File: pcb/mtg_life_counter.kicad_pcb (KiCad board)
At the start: 2 copper layers, 167.6 x 101.6 mm, 121 parts, among them J1 USB C 4907, J2 ICSP, J3 TP_UART, Q1 DMG2301L, Q10 DMG2301L, Q11 DMG2301L, Q12 DMG2301L, Q13 DMG2301L, Q14 DMG2301L, Q15 DMG2301L, Q16 DMG2301L, Q2 DMG2301L, Q3 DMG2301L, Q4 DMG2301L, Q5 DMG2301L, Q6 DMG2301L, Q7 DMG2301L, Q8 DMG2301L, Q9 DMG2301L, SW1 SW_SPST, SW2 SW_SPST, U1 ATmega328P-AU, U2 TPIC6C596, U3 TPIC6C596, U4 TPIC6C596, U5 TPIC6C596, Y1 16MHz

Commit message: start to route display traces
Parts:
- removed the R20 at (110.2, 36.0)
- removed the R33 at (174.9, 35.6)
- removed the R46 at (167.3, 167.2)
- removed R59: 10k, Resistor_SMD:R_0805_2012Metric_Pad1.20x1.40mm_HandSolder
- H1, H2, H3, H4: footprint MountingHole:MountingHole_3.2mm_M3_Pad_Via -> MountingHole:MountingHole_3.2mm_M3
- moved C7 116.2 mm to (189.2, 81.0), turned to -90 degrees
- moved H4 107.1 mm to (55.9, 147.3)
- moved C6 78.7 mm to (125.7, 81.0), turned to -90 degrees
- moved R47 65.8 mm to (139.1, 120.4), turned to -90 degrees
- moved R8 61.0 mm to (131.4, 82.8), turned to 90 degrees
- moved R9 59.9 mm to (134.0, 82.8), turned to 90 degrees
- moved C9 59.3 mm to (125.7, 119.1), turned to -90 degrees
- moved Q15 59.1 mm to (130.5, 127.3), turned to -90 degrees
- moved C8 59.1 mm to (189.2, 119.1), turned to -90 degrees
- moved R10 59.0 mm to (136.5, 82.8), turned to 90 degrees
- moved R46 58.7 mm to (131.4, 120.4), turned to -90 degrees
- moved R11 58.3 mm to (139.1, 82.8), turned to 90 degrees
- moved R45 58.0 mm to (134.0, 120.4), turned to -90 degrees
- moved R44 57.5 mm to (136.5, 120.4), turned to -90 degrees
- moved Q1 56.7 mm to (130.5, 75.9), turned to -90 degrees
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- renumbered C7 to C6, C6 to C7, D2 to D1, D3 to D2, D4 to D3, D5 to D4, D1 to D5, R21 to R20, R22 to R21, R23 to R22, R24 to R23, R25 to R24, R26 to R25, R27 to R26, R28 to R27, R29 to R28, R30 to R29, R31 to R30, R32 to R31, R34 to R32, R35 to R33, R36 to R34, R37 to R35, R38 to R36, R39 to R37, R40 to R38, R41 to R39, R42 to R40, R43 to R41, R44 to R42, R45 to R43, R47 to R44, R48 to R45, R49 to R46, R50 to R47, R51 to R48, R52 to R49, R53 to R50, R54 to R51, R55 to R52, R56 to R53, R57 to R54, R58 to R55
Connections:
- net /D1(TX) renamed /TX
- J3 pad 1: /D0(RX) -> unconnected-(J3-Pin_1-Pad1)
- U2 pad 7: Net-(U2-~{SRCLR}) -> +5V
- U3 pad 7: Net-(U3-~{SRCLR}) -> +5V
- U4 pad 7: Net-(U4-~{SRCLR}) -> +5V
- U5 pad 7: Net-(U5-~{SRCLR}) -> +5V
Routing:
- net +5V: track 0.00 -> 90.7 mm, vias 0 -> 2
- net /P2/CA1: track 0.00 -> 39.4 mm, vias 0 -> 2
- net /P4/CA1: track 0.00 -> 38.6 mm, vias 0 -> 2
- net /P1/CA3: track 0.00 -> 37.2 mm, vias 0 -> 2
- net /P3/CA3: track 0.00 -> 36.9 mm, vias 0 -> 2
- net /P3/CA4: track 0.00 -> 35.5 mm, vias 0 -> 2
- net /P1/CA4: track 0.00 -> 35.5 mm, vias 0 -> 2
- net Net-(Q12-G): track 0.00 -> 34.2 mm, vias 0 -> 2
- net /P1/CA2: track 0.00 -> 32.8 mm, vias 0 -> 2
- net /P2/SB: track 0.00 -> 32.8 mm, vias 0 -> 2
- net /P1/SB: track 0.00 -> 32.8 mm, vias 0 -> 2
- net /P3/CA2: track 0.00 -> 32.5 mm, vias 0 -> 2
- net /P2/CA2: track 0.00 -> 29.9 mm, vias 0 -> 2
- net /P2/SG: track 0.00 -> 29.8 mm, vias 0 -> 2
- net /P1/SG: track 0.00 -> 29.7 mm, vias 0 -> 2
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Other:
- board text added: "Max Proskauer v3.0 Jan 2026 github.com/mprosk/mtg_life_counter"
- board text added: "Version 3.0"
- board text removed: "Max Proskauer v2.0 Dec 2021 github.com/mprosk/mtg_life_counter"
- board text removed: "Version 2.0"

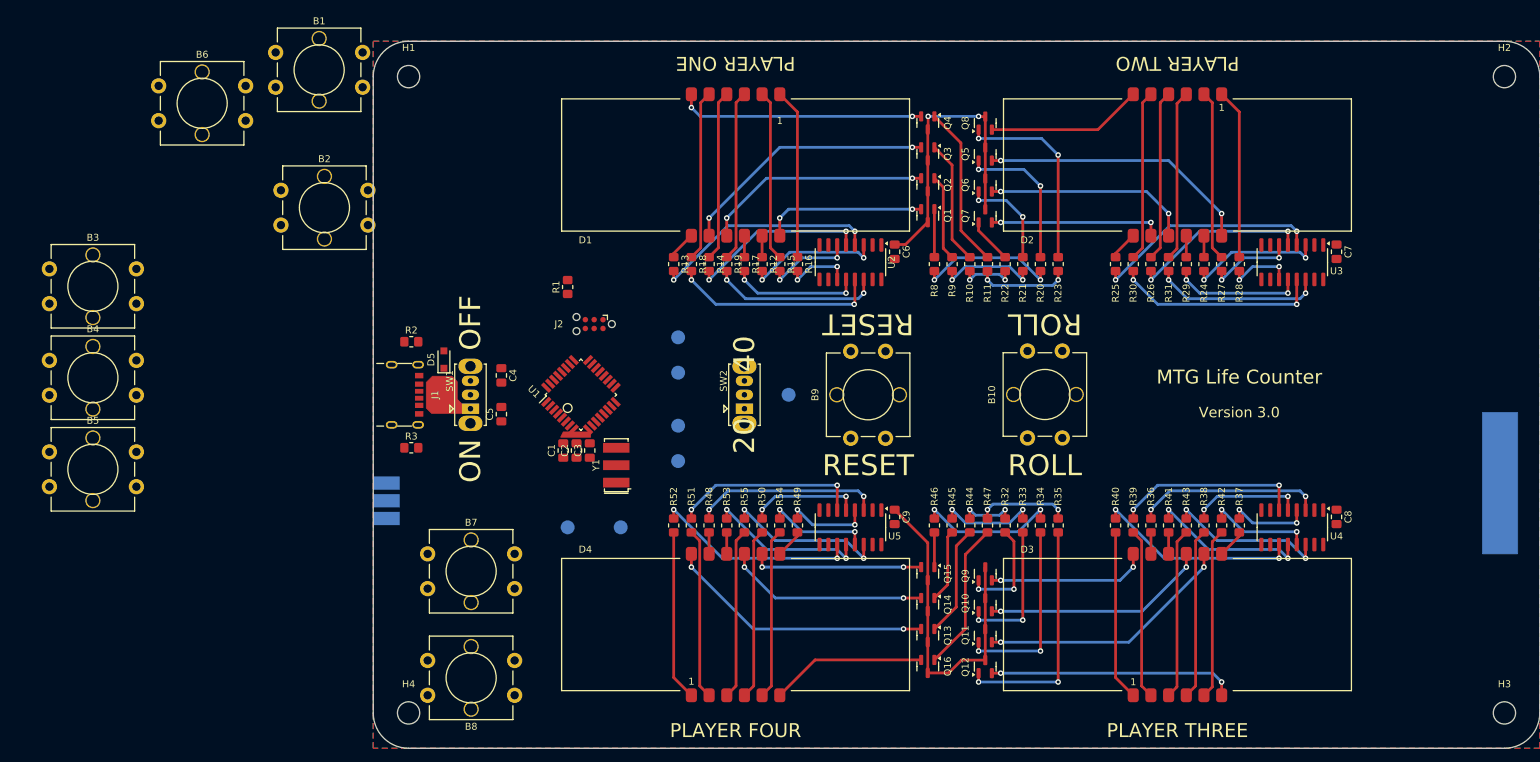
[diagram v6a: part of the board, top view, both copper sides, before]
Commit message: switch to all smd components
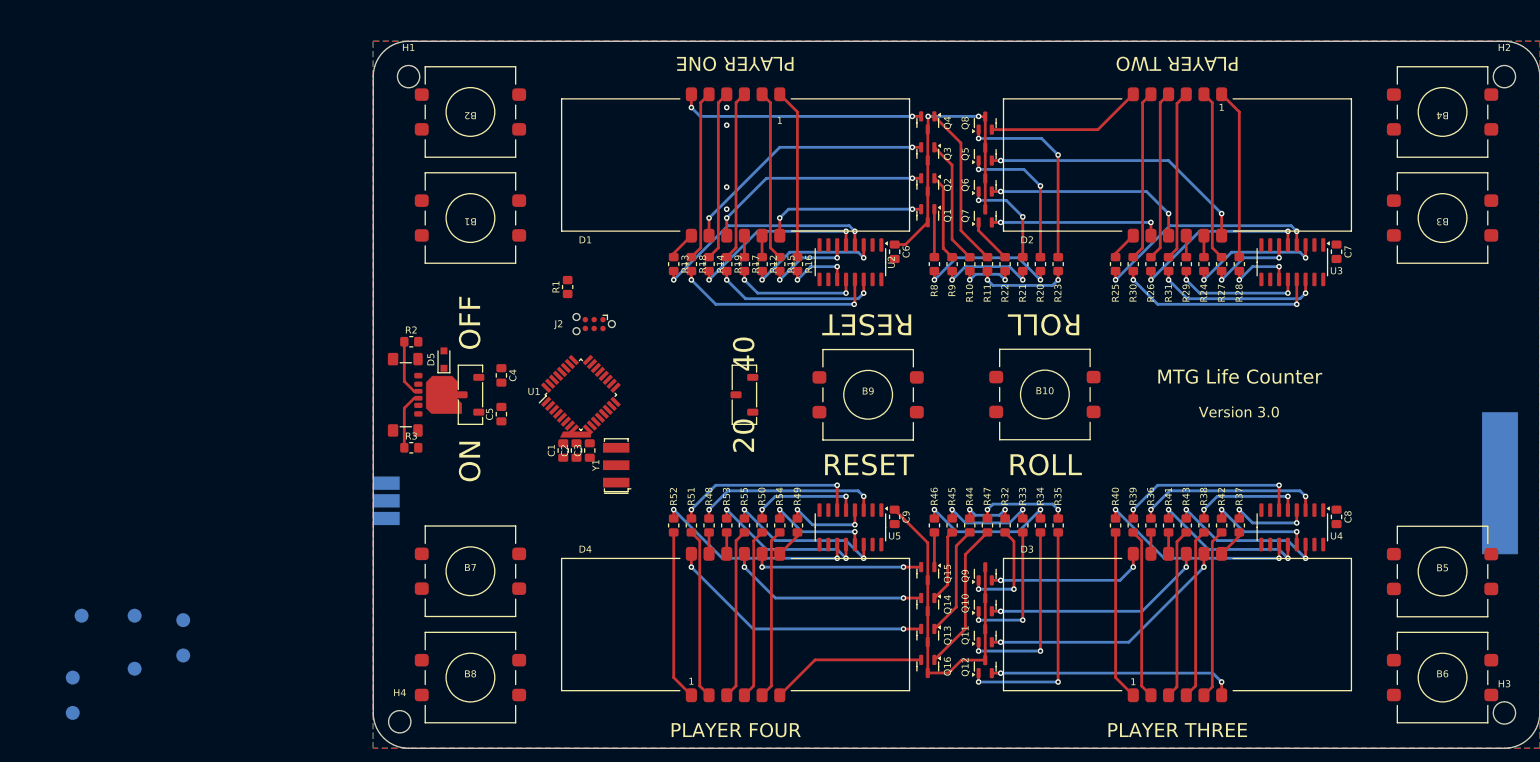
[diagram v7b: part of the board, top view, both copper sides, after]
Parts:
- B1, B10, B2, B3, B4, B5, B6, B7, B8, B9: footprint mtg_life_counter:B3F_12mm -> mtg_life_counter:SW_SPST_WE_WS-TASV_12mm_Tac
- J1: value USB C 4907 -> GCT USB-4135-GF-A; footprint mtg_life_counter:4907_USB_C_PowerOnly -> Connector_USB:USB_C_Receptacle_GCT_USB4135-GF-A_6P_TopMnt_Horizontal
- SW1, SW2: value SW_SPST -> MODE SW; footprint Button_Switch_THT:SW_Slide_SPDT_Straight_CK_OS102011MS2Q -> mtg_life_counter:SW_SPDT_CK_JS102011JCQN
- moved B4 197.7 mm to (204.5, 61.0), turned to 180 degrees
- moved B6 196.4 mm to (204.5, 142.2)
- moved B5 194.5 mm to (204.5, 127.0)
- moved B3 194.2 mm to (204.5, 76.2), turned to 180 degrees
- moved TP6 101.9 mm to (16.5, 141.0)
- moved TP3 94.2 mm to (7.62, 142.2)
- moved TP4 94.2 mm to (7.62, 147.3)
- moved TP1 81.9 mm to (23.5, 134.0)
- moved TP2 81.9 mm to (23.5, 139.1)
- moved TP5 71.0 mm to (8.89, 133.3)
- moved TP7 71.0 mm to (16.5, 133.3)
- moved B1 30.4 mm to (64.8, 76.2), turned to 180 degrees
- moved B2 25.1 mm to (64.8, 61.0), turned to 180 degrees
- moved J1 3.45 mm to (54.3, 101.6)
- moved SW1 2.00 mm to (64.8, 101.6)
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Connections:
- SW1 pad 1: VBUS -> +5V
- SW1 pad 2: +5V -> VBUS
- SW1 pad 3: (no net) -> unconnected-(SW1-C-Pad3)
- SW2 pad 1: /MODE_SW -> GND
- SW2 pad 2: GND -> /MODE_SW
- SW2 pad 3: (no net) -> unconnected-(SW2-C-Pad3)
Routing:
- net Net-(J1-CC2): track 0.00 -> 8.31 mm
- net Net-(J1-CC1): track 0.00 -> 8.31 mm
- net GND: vias 0 -> 4

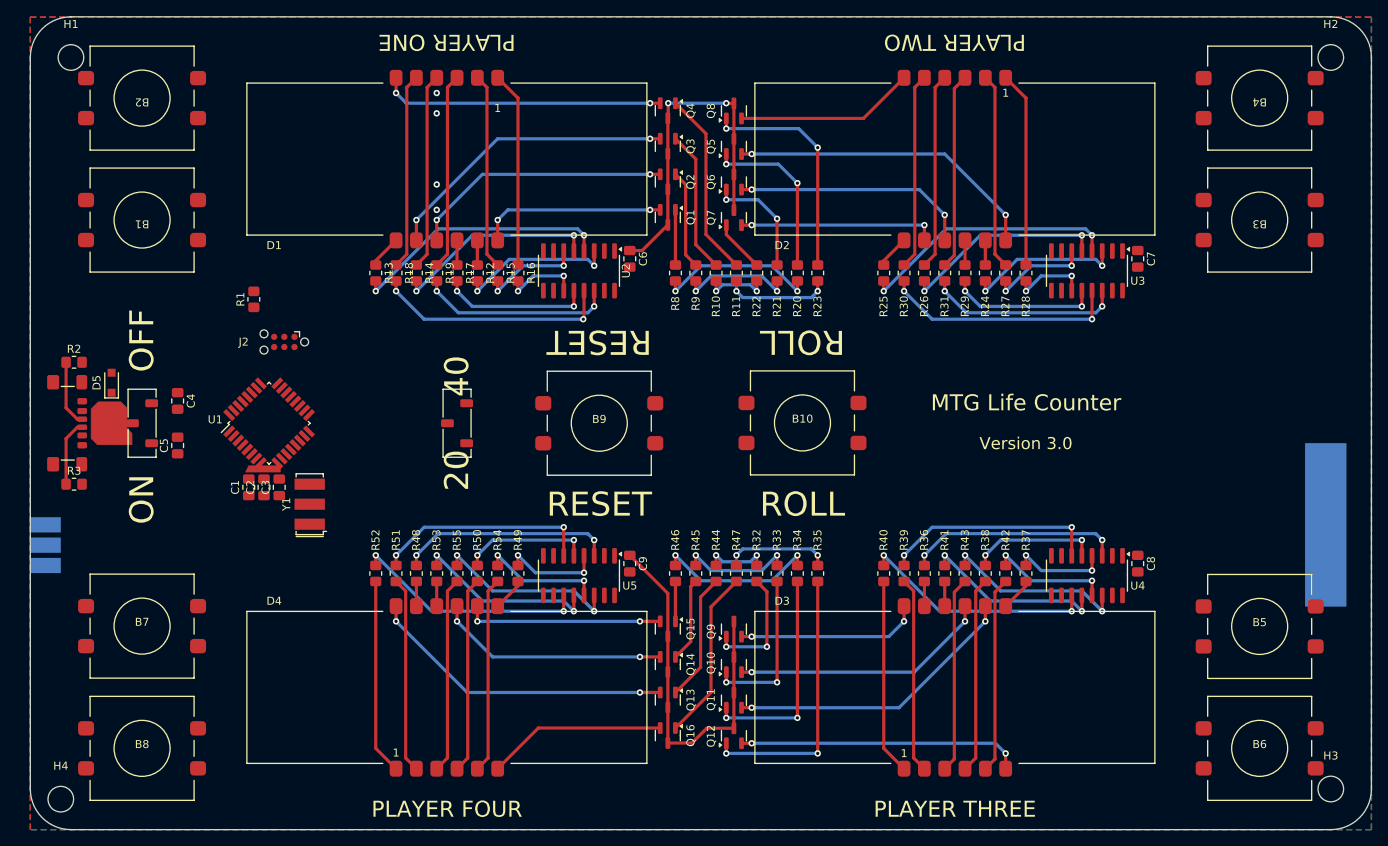
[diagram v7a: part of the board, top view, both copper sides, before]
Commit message: continue layout. improve 3d model
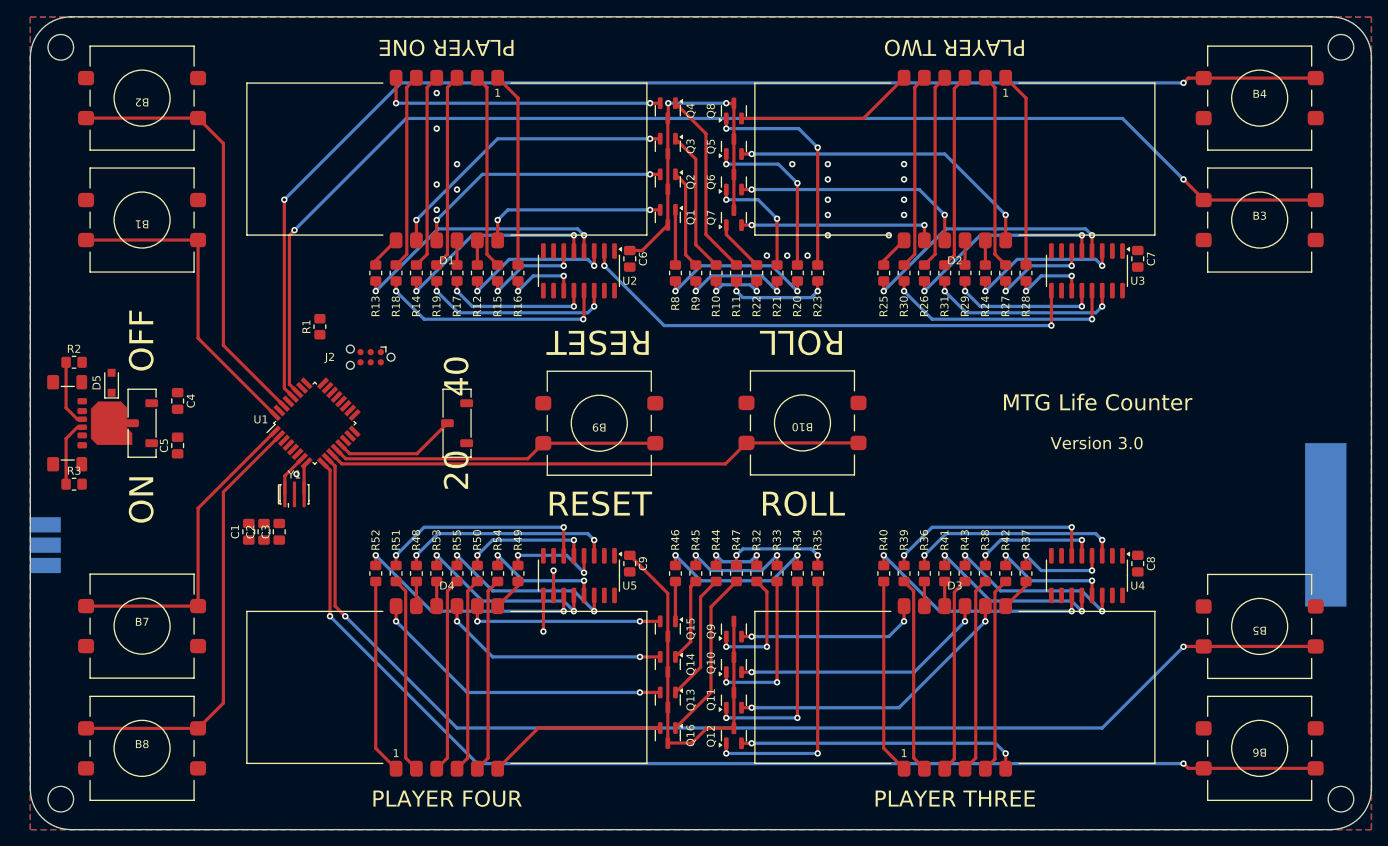
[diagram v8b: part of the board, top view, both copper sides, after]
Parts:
- D1: footprint mtg_life_counter:KW4-S561xxB_SMD -> mtg_life_counter:KW4-S561xVB_SMD
- D2: footprint mtg_life_counter:KW4-S561xxB_SMD -> mtg_life_counter:KW4-S561xGB_SMD
- D3: footprint mtg_life_counter:KW4-S561xxB_SMD -> mtg_life_counter:KW4-S561xAB_SMD
- D4: footprint mtg_life_counter:KW4-S561xxB_SMD -> mtg_life_counter:KW4-S561xBB_SMD
- Y1: footprint Crystal:Resonator_SMD-3Pin_7.2x3.0mm -> Crystal:Resonator_SMD_Murata_CSTxExxV-3Pin_3.0x1.1mm_HandSoldering
- moved J2 11.0 mm to (93.3, 93.3)
- moved R1 8.94 mm to (87.0, 89.5)
- moved U1 5.72 mm to (86.4, 101.6)
- moved C1 5.56 mm to (78.1, 115.2)
- moved C2 5.56 mm to (80.0, 115.2)
- moved C3 5.56 mm to (81.9, 115.2)
- moved Y1 2.27 mm to (83.8, 110.5), turned to 0 degrees
- moved H1 1.80 mm to (54.6, 54.6)
- moved H3 1.80 mm to (214.6, 148.6)
- moved H2 1.80 mm to (214.6, 54.6)
- turned B10 to 180 degrees
- turned B3 to 0 degrees
- turned B4 to 0 degrees
- turned B5 to 180 degrees
- turned B6 to 180 degrees
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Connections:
- net Net-(U1-XTAL1(PB6)) renamed /XTAL1
- net Net-(U1-XTAL2(PB7)) renamed /XTAL2
- U1 pad 1: /BTN_P1_DN -> /BTN_P4_UP
- U1 pad 11: /BTN_P3_DN -> /BTN_ROLL
- U1 pad 2: /BTN_P2_UP -> /BTN_P4_DN
- U1 pad 23: /BTN_P4_UP -> /DIGIT_SEL_1
- U1 pad 24: /BTN_P4_DN -> /DIGIT_SEL_2
- U1 pad 25: /DIGIT_SEL_1 -> /DIGIT_SEL_3
- U1 pad 26: /DIGIT_SEL_2 -> /DIGIT_SEL_4
- U1 pad 27: /DIGIT_SEL_3 -> /BTN_P2_UP
- U1 pad 28: /DIGIT_SEL_4 -> /BTN_P2_DN
- U1 pad 30: /BTN_ROLL -> /BTN_P1_DN
- U1 pad 9: /BTN_P2_DN -> /BTN_P3_DN
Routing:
- net /BTN_P2_DN: track 0.00 -> 160.3 mm, vias 0 -> 2
- net /BTN_P2_UP: track 0.00 -> 158.7 mm, vias 0 -> 2
- net /BTN_P3_UP: track 0.00 -> 151.9 mm, vias 0 -> 2
- net /BTN_P3_DN: track 0.00 -> 150.6 mm, vias 0 -> 2
- net /BTN_ROLL: track 0.00 -> 67.4 mm
- net /SHIFT_CARRY_3: track 0.00 -> 65.2 mm, vias 0 -> 2
- net /BTN_P4_DN: track 0.00 -> 54.8 mm
- net /BTN_P1_DN: track 0.00 -> 54.4 mm
- net /BTN_RESET: track 0.00 -> 41.1 mm
- net /BTN_P1_UP: track 0.00 -> 39.9 mm
- net /BTN_P4_UP: track 0.00 -> 39.8 mm
- net /MODE_SW: track 0.00 -> 15.3 mm
- net /XTAL1: track 0.00 -> 5.36 mm
- net /SHIFT_CARRY_1: track 0.00 -> 4.51 mm, vias 0 -> 1
- net /XTAL2: track 0.00 -> 4.04 mm
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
